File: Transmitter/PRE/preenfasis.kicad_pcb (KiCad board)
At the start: 2 copper layers, 25 x 40 mm, 24 parts, among them J1 SMA H, J2 SMA H, J3 SMA H, J4 SMA H

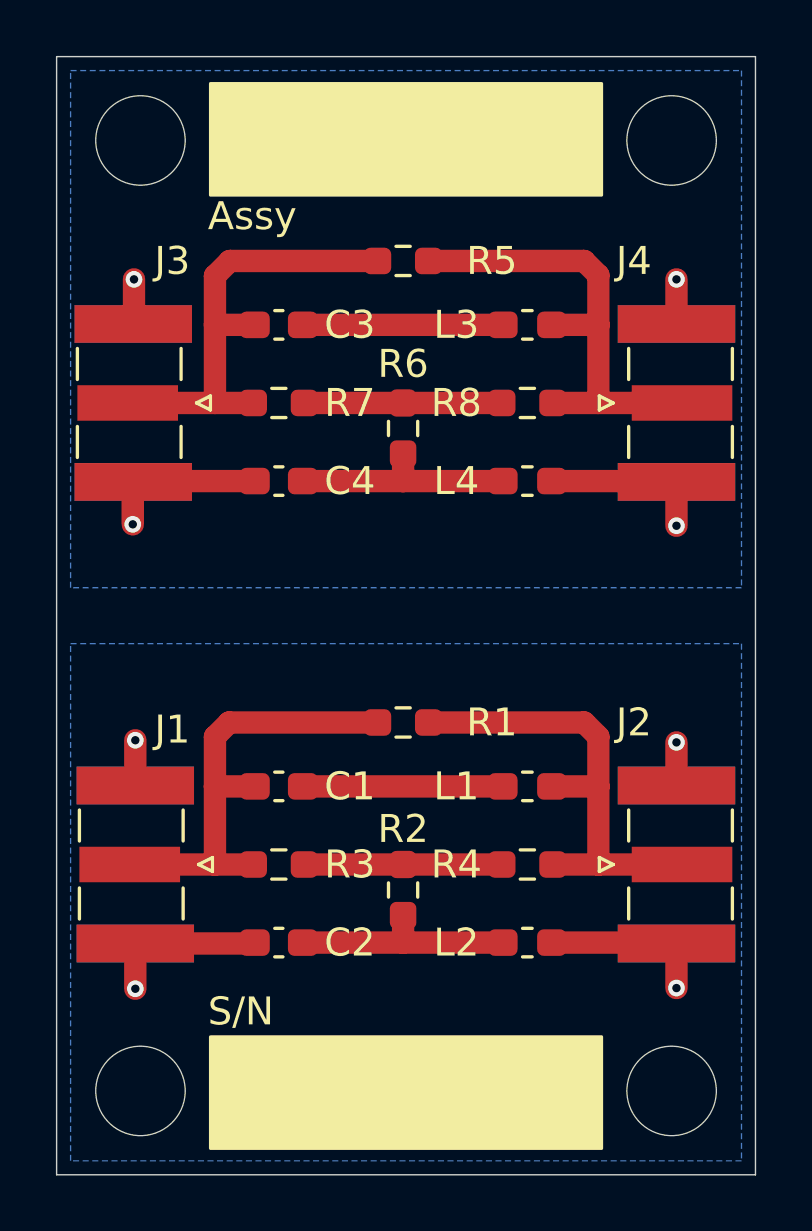
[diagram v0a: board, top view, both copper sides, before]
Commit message: Add CPW to preenfasis and tx amplifier
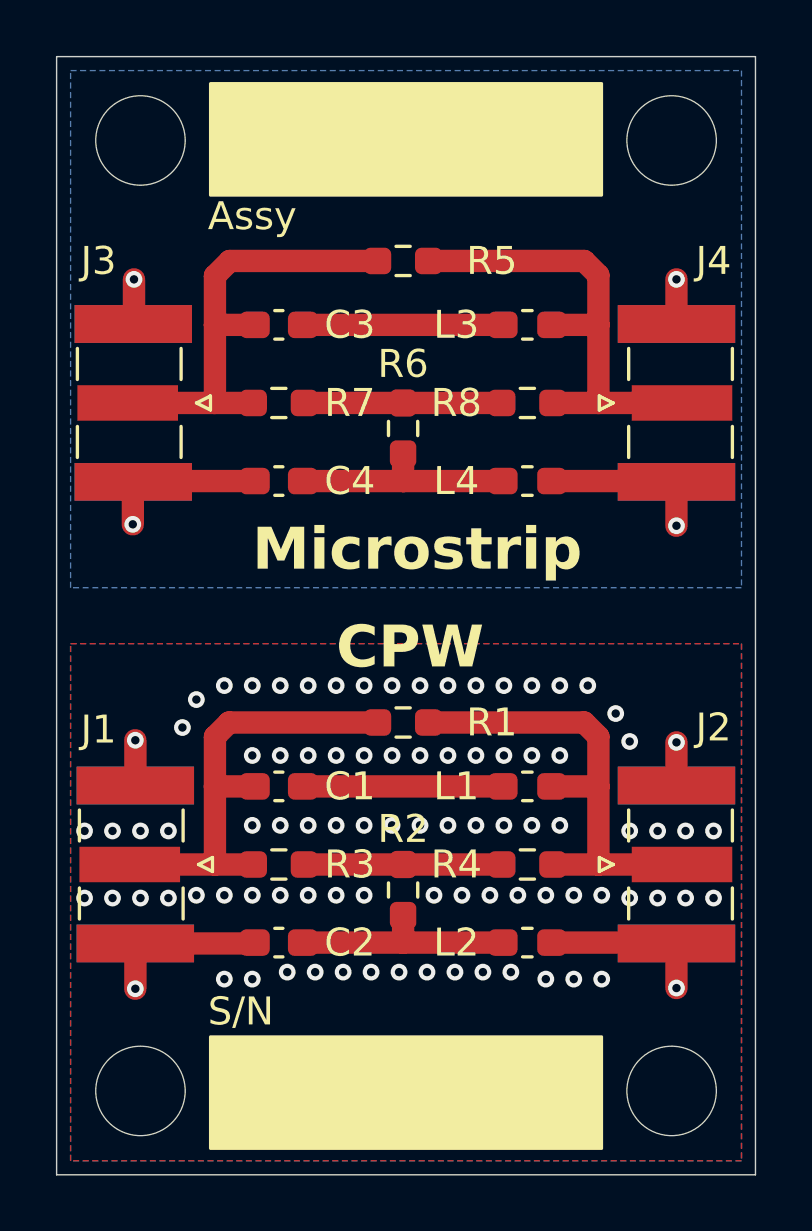
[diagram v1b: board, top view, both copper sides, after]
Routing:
- net Net-(J1-Ext): vias 4 -> 90
- added copper zone on F.Cu, net Net-(J1-Ext)
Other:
- board text added: "CPW"
- board text added: "Microstrip"
